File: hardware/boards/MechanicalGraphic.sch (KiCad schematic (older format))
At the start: 1 part

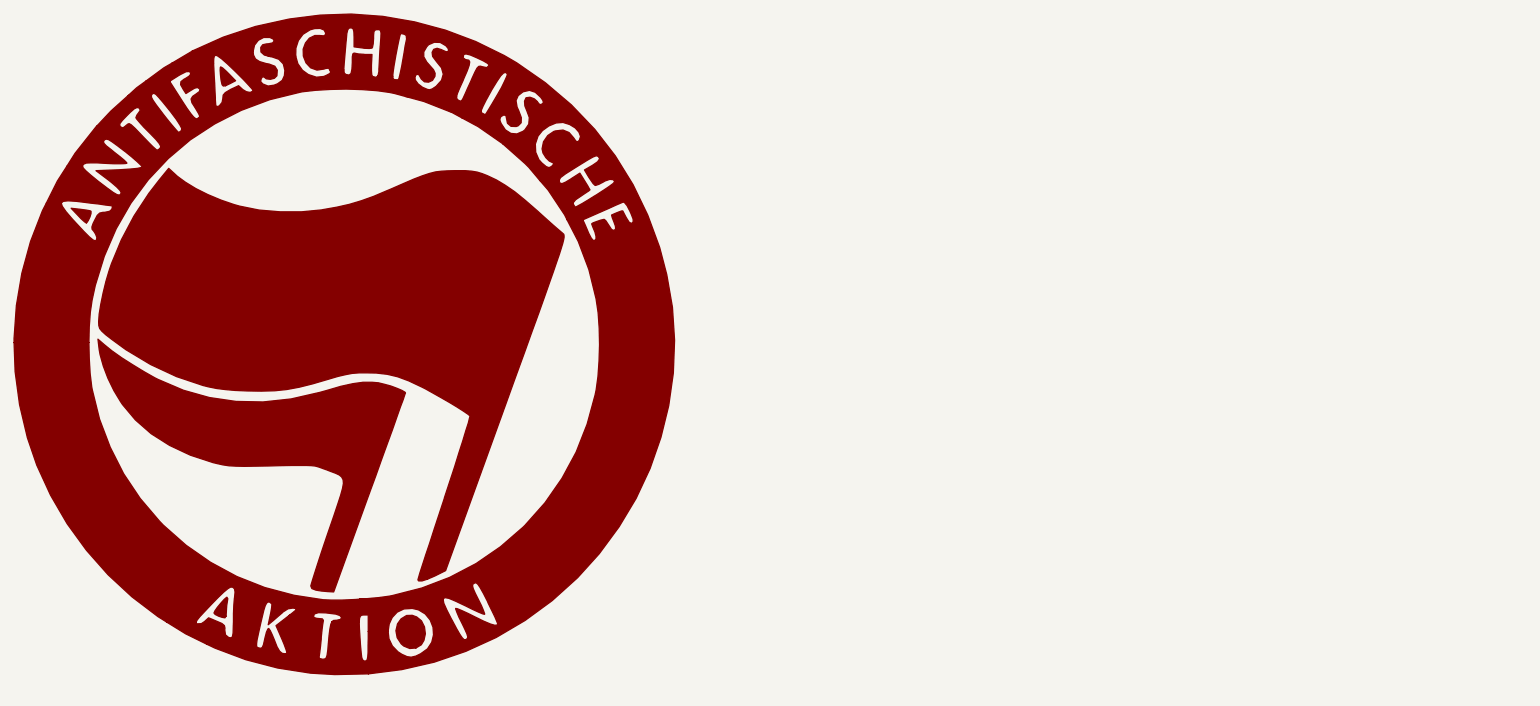
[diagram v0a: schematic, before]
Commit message: Upped the schematic frame size from A4 to A3 to allow for some more breathing room, it was getting stuff in the powersupply schematic
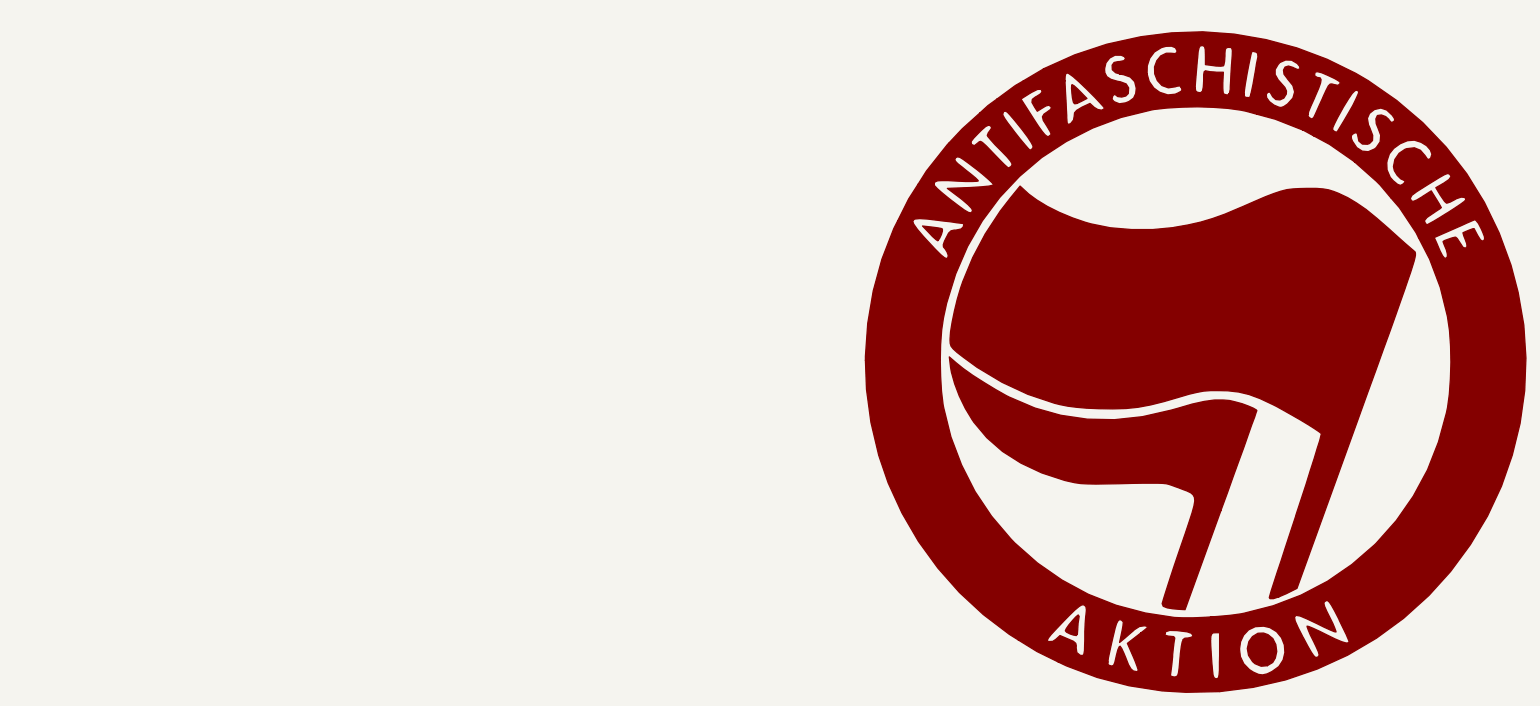
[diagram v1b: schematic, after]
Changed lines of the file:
@@
 EELAYER 30 0
 EELAYER END
-$Descr A4 11693 8268
+$Descr A3 16535 11693
 encoding utf-8
 Sheet 11 11
@@
 L lethalbit-graphics:Antifaschistische_Aktion G1
 U 1 1 5EE64E35
-P 9250 450
-F 0 "G1" H 11143 -1458 50  0001 L CNN
-F 1 "Antifaschistische_Aktion" H 11143 -1549 50  0001 L CNN
-F 2 "lethalbit-graphics:Antifaschistische Aktion_100dpi" H 9200 600 50  0001 C CNN
-F 3 "" H 9200 600 50  0001 C CNN
-	1    9250 450
+P 14050 550
+F 0 "G1" H 15943 -1358 50  0001 L CNN
+F 1 "Antifaschistische_Aktion" H 15943 -1449 50  0001 L CNN
+F 2 "lethalbit-graphics:Antifaschistische Aktion_100dpi" H 14000 700 50  0001 C CNN
+F 3 "" H 14000 700 50  0001 C CNN
+	1    14050 550
 	1    0    0    -1
 $EndComp
